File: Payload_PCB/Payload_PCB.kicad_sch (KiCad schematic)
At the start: 26 parts, among them J1 Conn_01x06_Pin, Q1 NMOS, Q2 NMOS, Q3 NMOS, Q4 PMOS, Q5 PMOS, Q6 NMOS, U1 TSR_1-2450

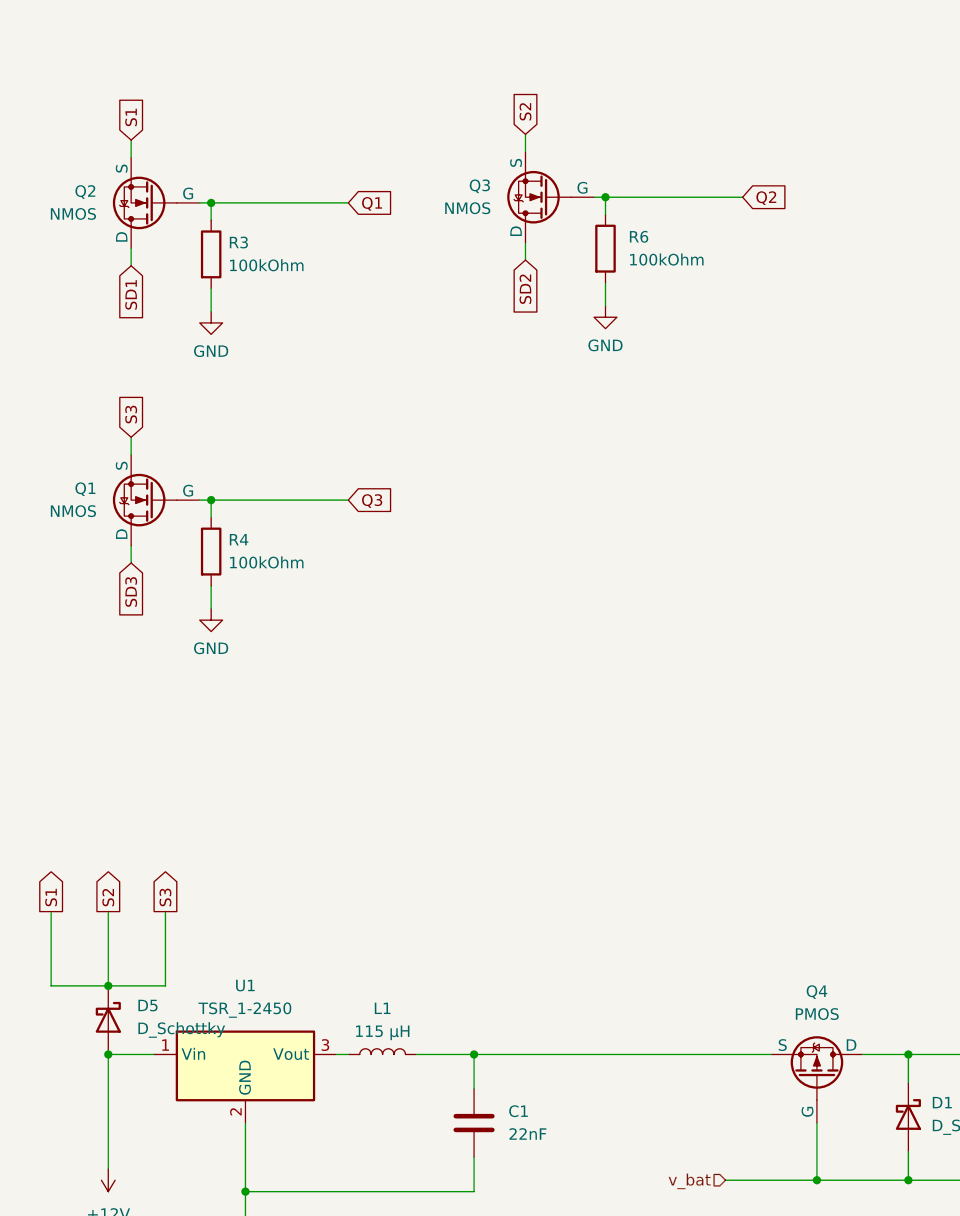
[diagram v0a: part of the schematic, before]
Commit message: Changed solenoid control: Now using capacities
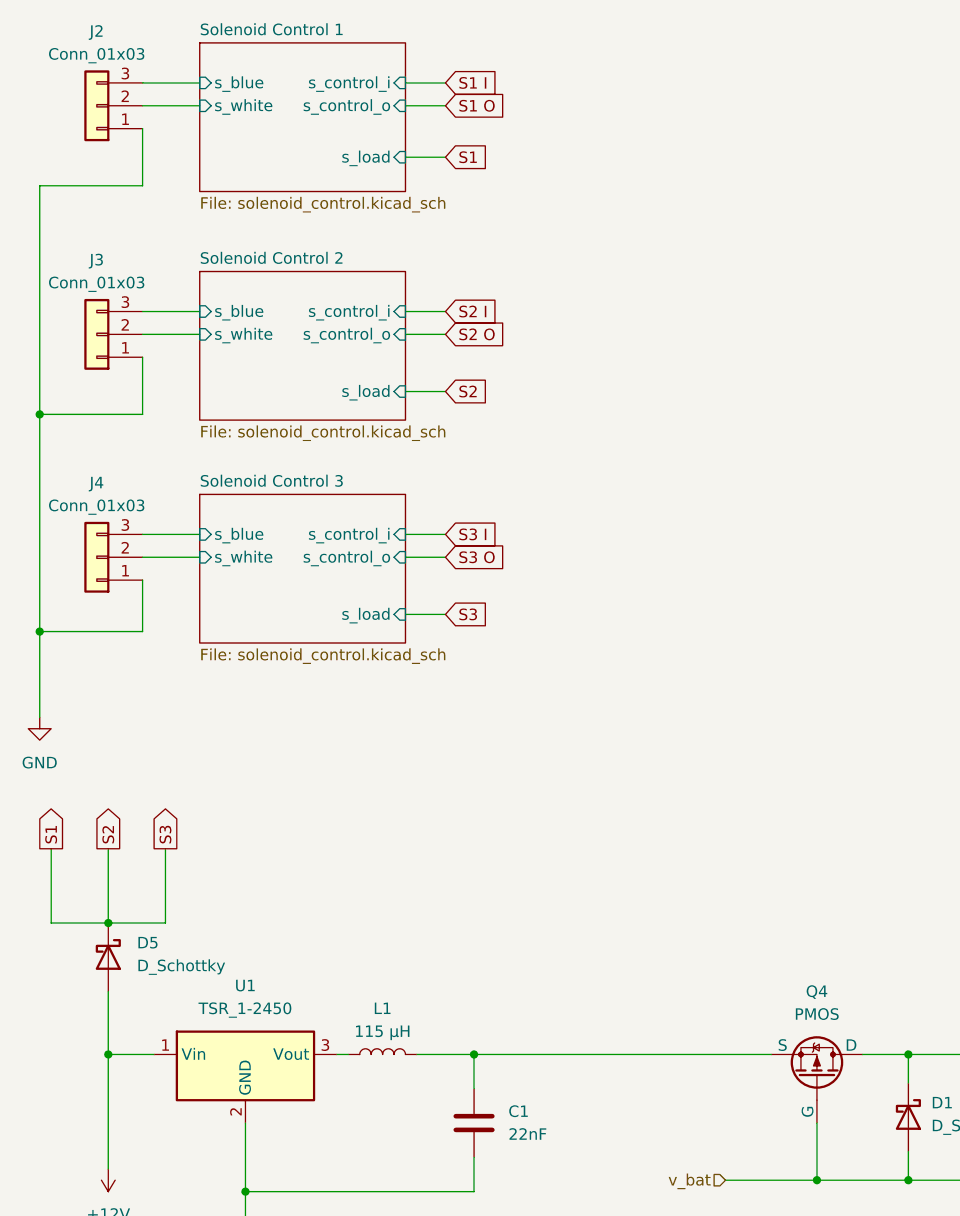
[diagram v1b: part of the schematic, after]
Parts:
- removed Q1, Q2, Q3: NMOS, symbol Simulation_SPICE:NMOS
- removed R3, R4, R6: 100kOhm, symbol Device:R
- added J2, J3, J4: Conn_01x03, symbol Connector_Generic:Conn_01x03
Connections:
- net GND: now also J2.1 (Pin_1), J3.1 (Pin_1), J4.1 (Pin_1)
- new net Solenoid Control 1/s_blue: J2.3 (Pin_3)
- new net Solenoid Control 1/s_white: J2.2 (Pin_2)
- new net Solenoid Control 2/s_blue: J3.3 (Pin_3)
- new net Solenoid Control 2/s_white: J3.2 (Pin_2)
- new net Solenoid Control 3/s_blue: J4.3 (Pin_3)
- new net Solenoid Control 3/s_white: J4.2 (Pin_2)
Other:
- added sheet Solenoid Control 1 (solenoid_control.kicad_sch)
- added sheet Solenoid Control 2 (solenoid_control.kicad_sch)
- added sheet Solenoid Control 3 (solenoid_control.kicad_sch)
- moved on the sheet: D5

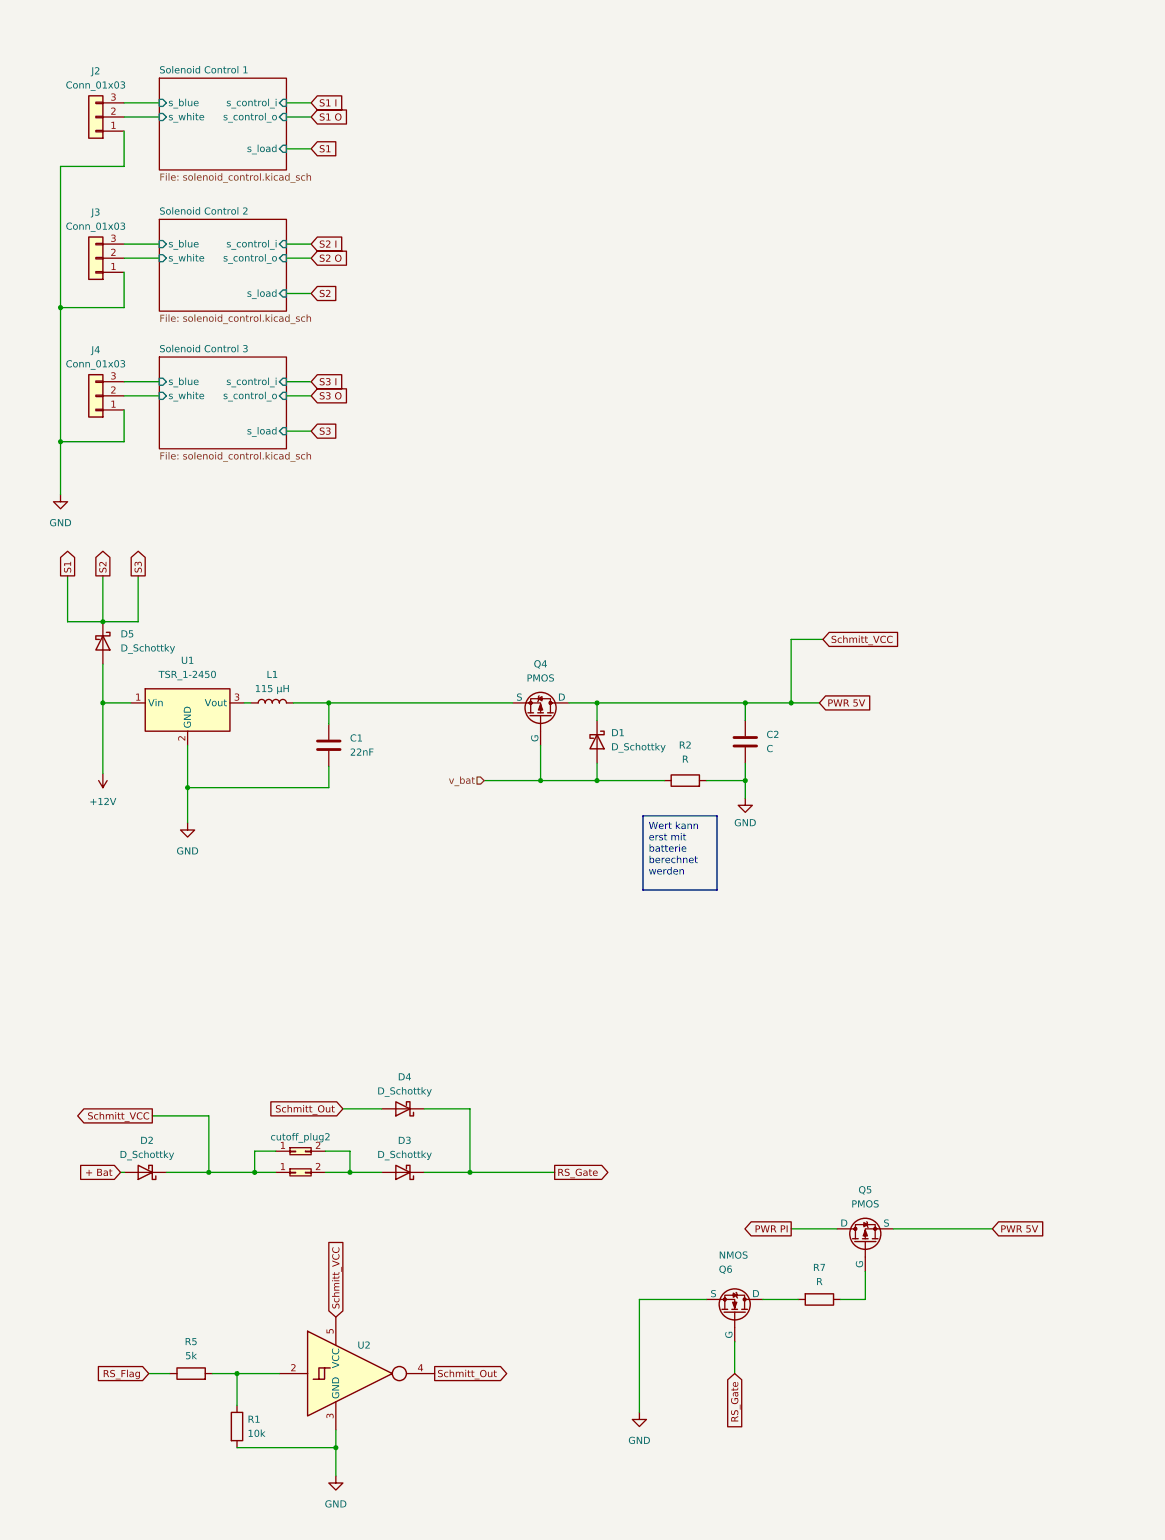
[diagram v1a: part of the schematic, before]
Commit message: Added Symbols and Footprints
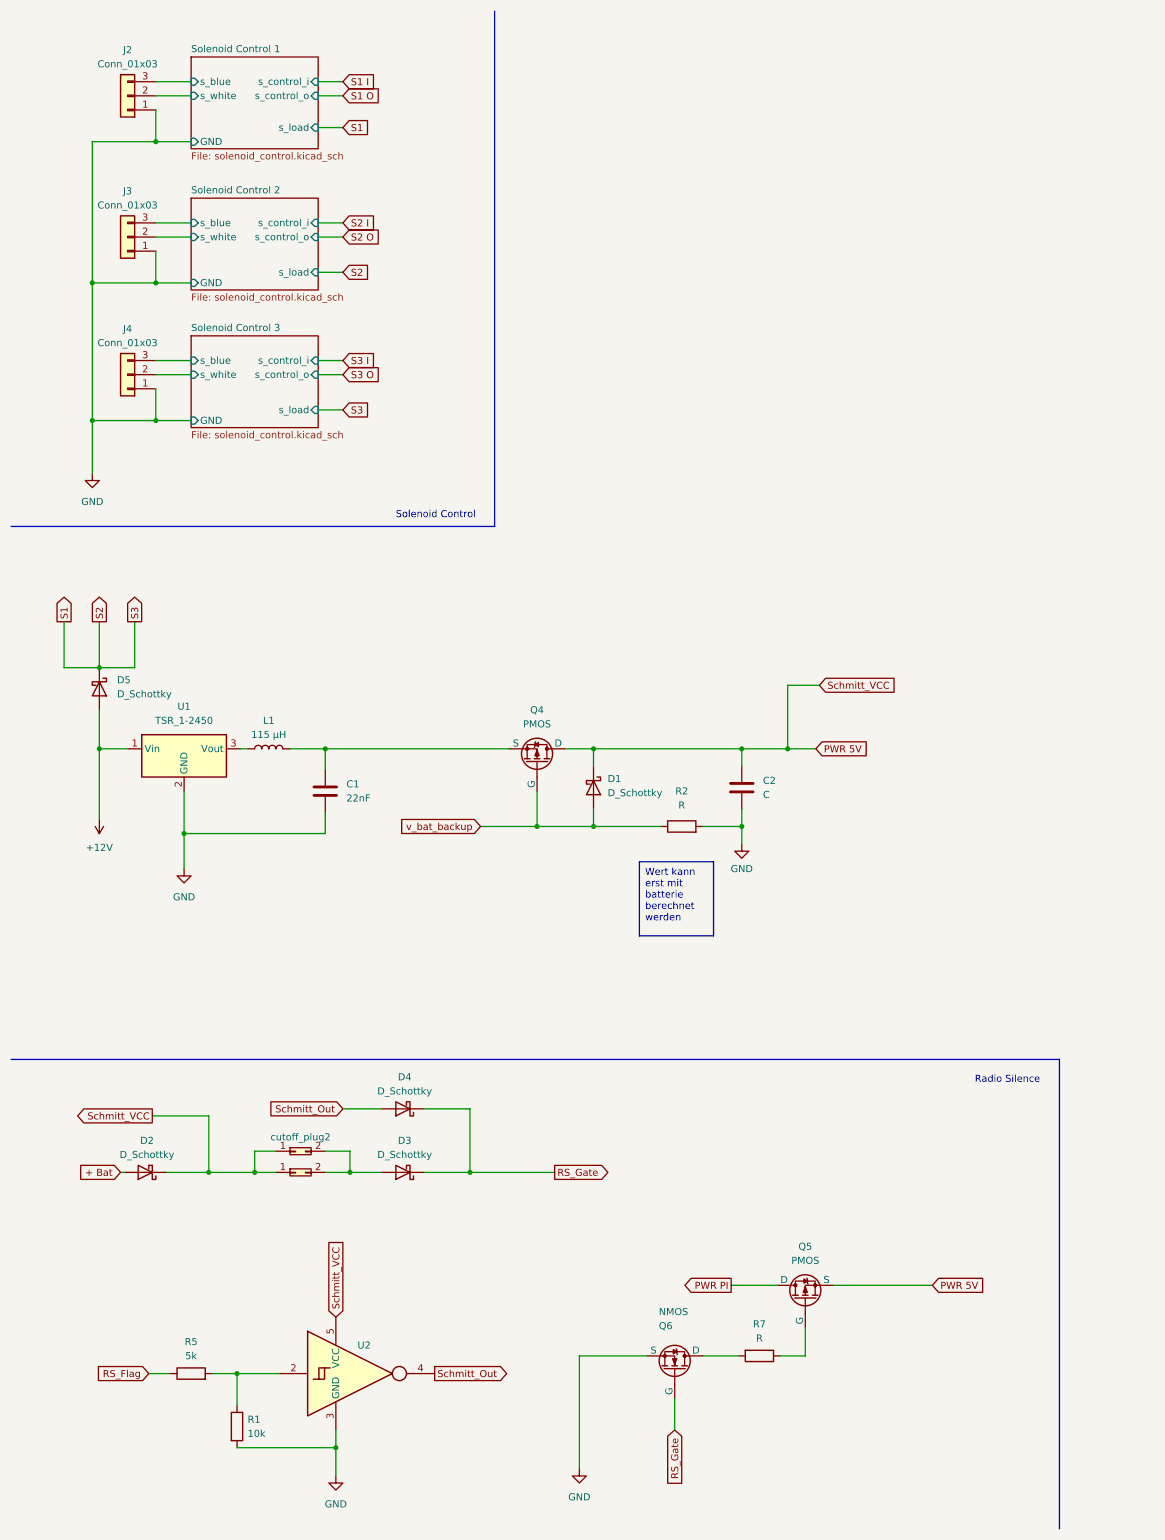
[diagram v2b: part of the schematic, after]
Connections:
- net v_bat renamed v_bat_backup
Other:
- sheet Solenoid Control 1 ports: added GND; removed none
- sheet Solenoid Control 2 ports: added GND; removed none
- sheet Solenoid Control 3 ports: added GND; removed none
- note added: "Radio Silence"
- note added: "Solenoid Control"
- moved on the sheet: C1, C2, D1, D5, J2, J3, J4, L1, Q4, Q5, Q6, R2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

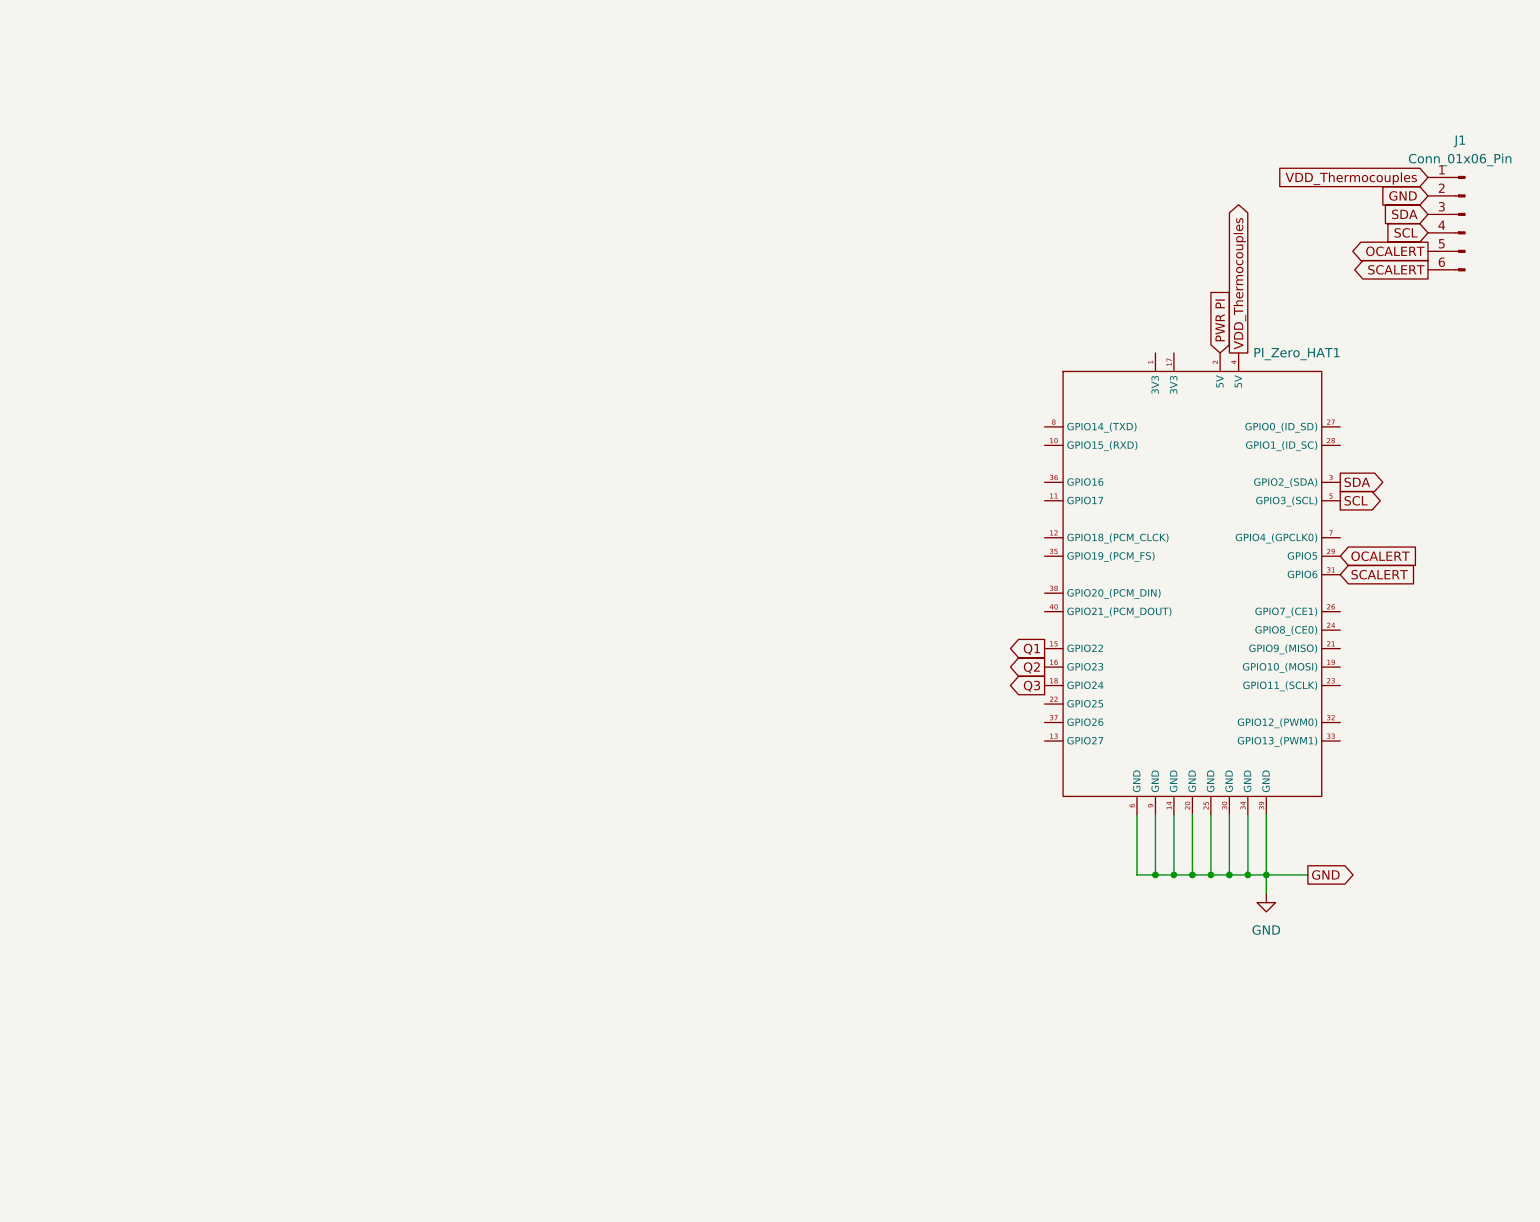
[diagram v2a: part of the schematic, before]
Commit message: Added BHI160 as accelerator and merged two KiCad Projects
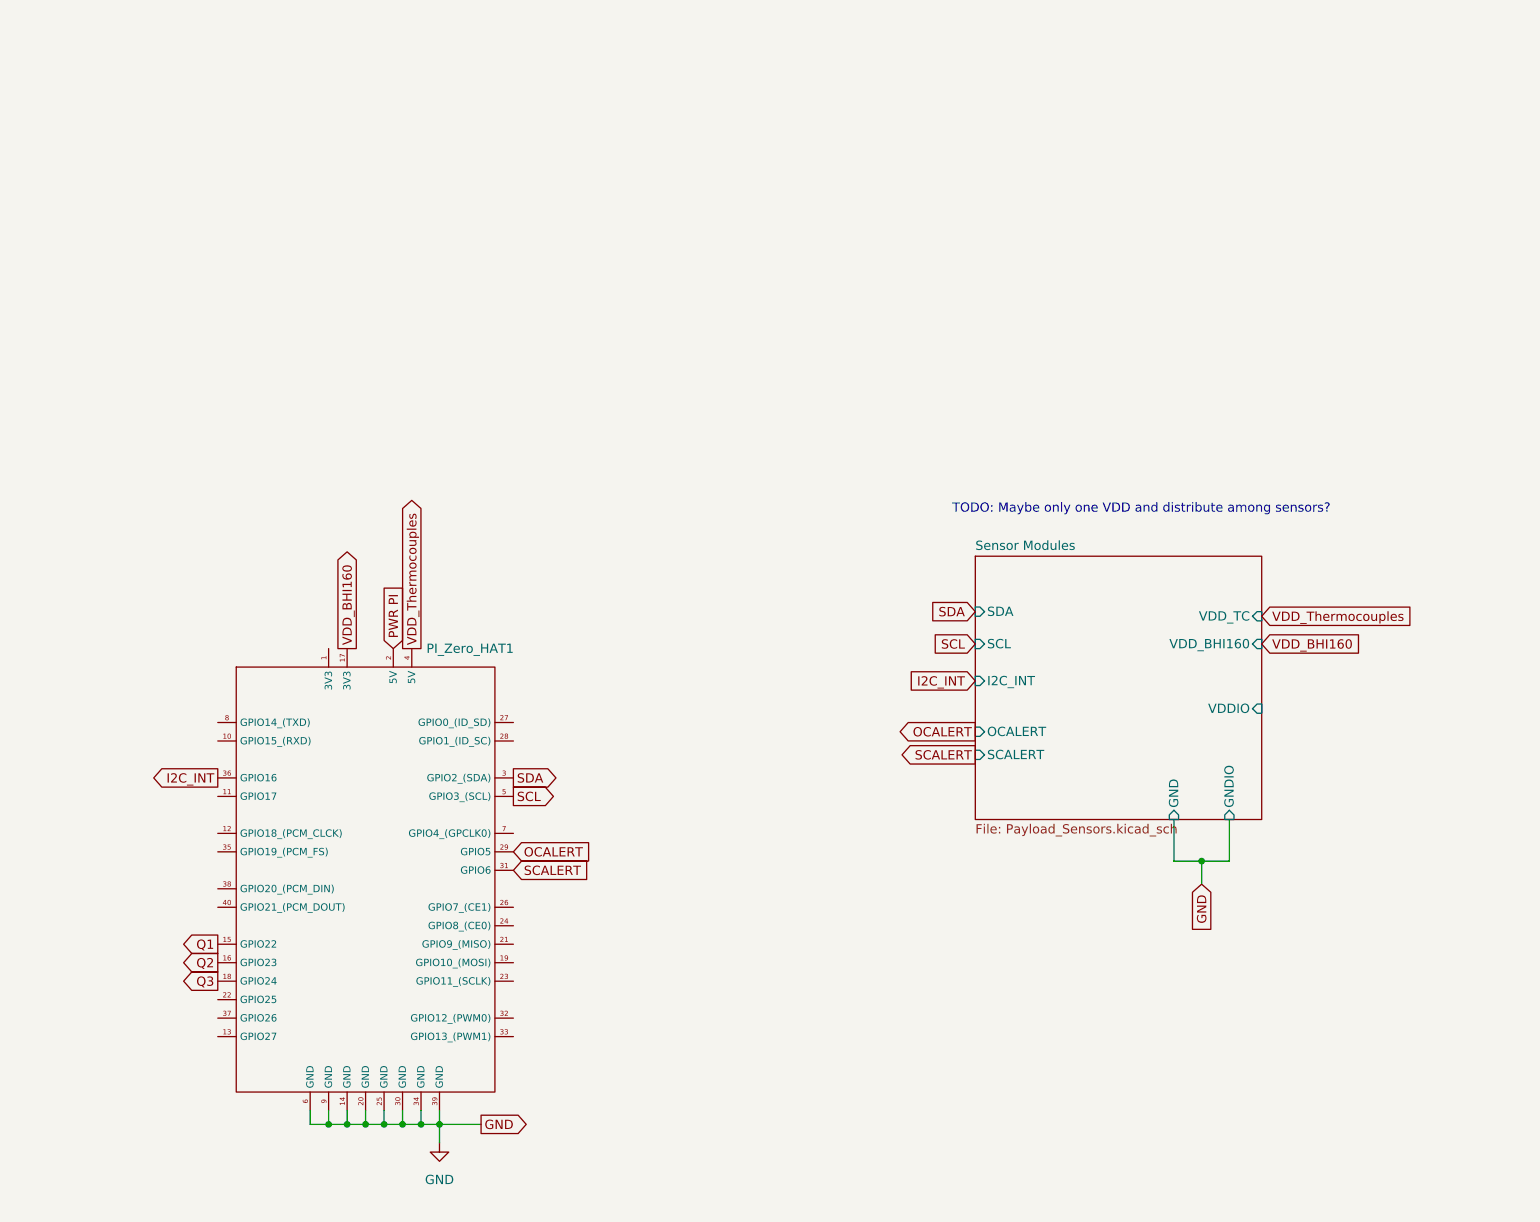
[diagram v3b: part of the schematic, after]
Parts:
- removed J1: Conn_01x06_Pin, symbol Connector:Conn_01x06_Pin
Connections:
- net VDD_BHI160: now reaches PI_Zero_HAT1.17 (3V3)
- net I2C_INT: now reaches PI_Zero_HAT1.36 (GPIO16)
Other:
- added sheet Sensor Modules (Payload_Sensors.kicad_sch)
- note added: "TODO: Maybe only one VDD and distribute among sensors?"
- moved on the sheet: PI_Zero_HAT1
